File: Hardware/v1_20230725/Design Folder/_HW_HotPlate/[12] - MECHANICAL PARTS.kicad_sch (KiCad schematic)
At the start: 15 parts, among them P1201 CONN_HDR_8POS_2ROW_2.54MM_RA

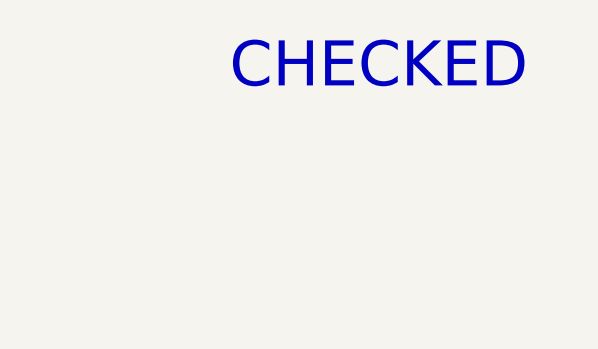
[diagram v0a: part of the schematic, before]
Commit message: Schematic library has been updated
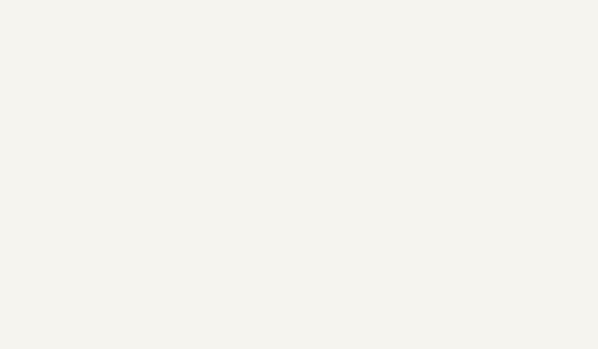
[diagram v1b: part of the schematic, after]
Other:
- note removed: "CHECKED"
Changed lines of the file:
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@@
 (kicad_sch (version 20230121) (generator eeschema)
-  (paper "B")
+  (paper "C")
   (title_block
     (title "Hot Plate")
@@
     (company "Mend0z0")
     (comment 1 "v1")
+    (comment 2 "RELEASED")
     (comment 3 "Siavash Taher Parvar")
     (comment 8 "N/A")
@@
     (effects (font (size 5 5)) (justify left bottom))
   )
-  (text "CHECKED" (at 381 36.83 0)
-    (effects (font (size 5 5)) (justify left bottom))
-  )

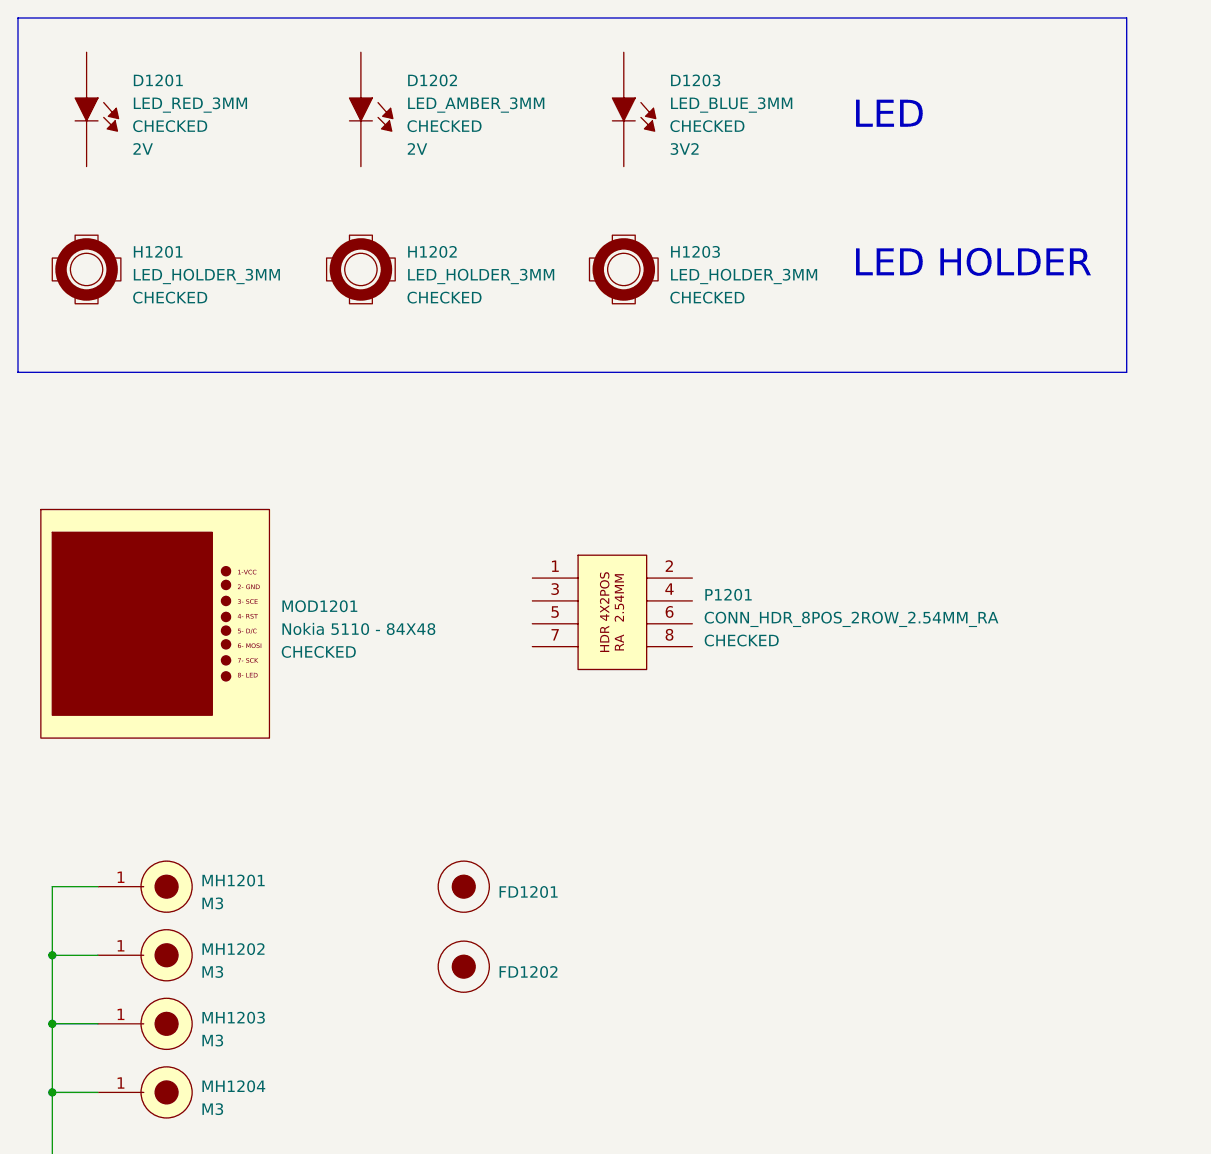
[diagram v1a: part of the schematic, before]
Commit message: components have been updated
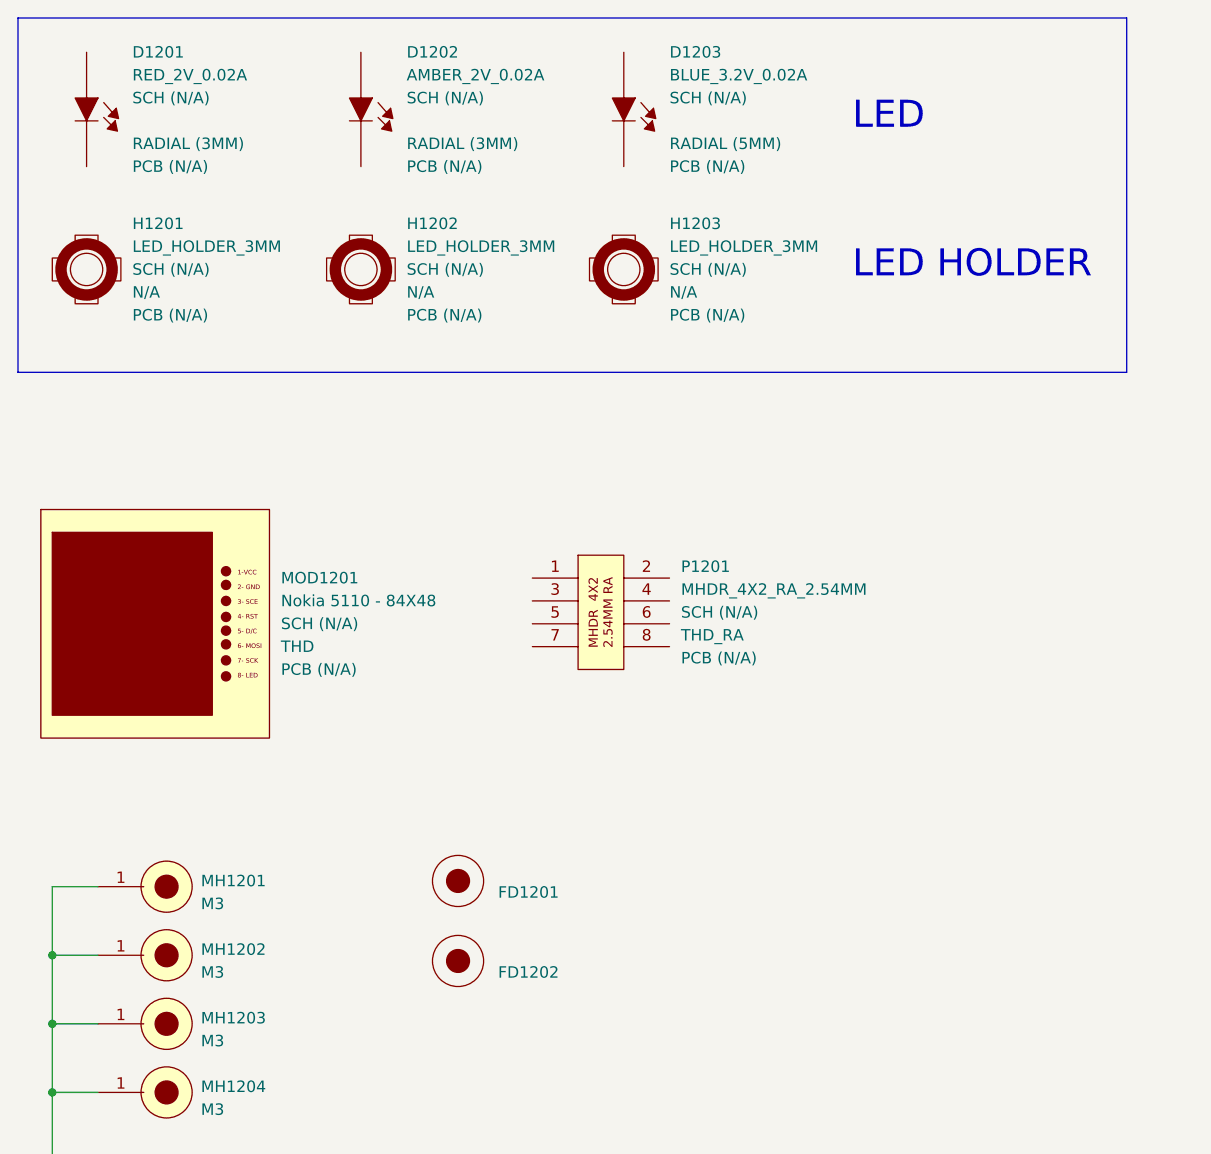
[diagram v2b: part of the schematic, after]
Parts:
- D1201: value LED_RED_3MM -> RED_2V_0.02A; footprint (none) -> LED_THT:LED_D3.0mm; symbol _SCHLIB_HotPlate:MECH_LED_RED_3MM -> _SCHLIB_HotPlate:DIODE_LED_RED_2V_0.02A_627nm_RADIAL (3MM); Manufacturer (none) -> Kingbright; PCB CHECk (none) -> PCB (N/A); Package (none) -> RADIAL (3MM); Part Number WP7113ID -> (none); Part Number (Manufacturer) (none) -> WP7113ID; Part Number (Vendor) (none) -> 754-1264-ND; SCH CHECK CHECKED -> SCH (N/A); Vendor (none) -> Digikey; Voltage 2V -> (none)
- D1202: value LED_AMBER_3MM -> AMBER_2V_0.02A; footprint (none) -> LED_THT:LED_D3.0mm; symbol _SCHLIB_HotPlate:MECH_LED_AMBER_3MM -> _SCHLIB_HotPlate:DIODE_LED_AMBER_2V_0.02A_610nm_RADIAL (3MM); Manufacturer (none) -> American Bright Optoelectronics Corporation; PCB CHECk (none) -> PCB (N/A); Package (none) -> RADIAL (3MM); Part Number BL-BJC1V4V-AT -> (none); Part Number (Manufacturer) (none) -> BL-BJC1V4V-AT; Part Number (Vendor) (none) -> BL-BJC1V4V-AT-ND; SCH CHECK CHECKED -> SCH (N/A); Vendor (none) -> Digikey; Voltage 2V -> (none)
- D1203: value LED_BLUE_3MM -> BLUE_3.2V_0.02A; footprint (none) -> LED_THT:LED_D5.0mm; symbol _SCHLIB_HotPlate:MECH_LED_BLUE_3MM -> _SCHLIB_HotPlate:DIODE_LED_BLUE_3.2V_0.02A_465nm_RADIAL (5MM); Manufacturer (none) -> Würth Elektronik; PCB CHECk (none) -> PCB (N/A); Package (none) -> RADIAL (5MM); Part Number 151051BS04000 -> (none); Part Number (Manufacturer) (none) -> 151051BS04000; Part Number (Vendor) (none) -> 732-5015-ND; SCH CHECK CHECKED -> SCH (N/A); Vendor (none) -> Digikey; Voltage 3V2 -> (none)
- FD1201, FD1202, TXT1201: value ~ -> (none)
- H1201, H1202, H1203: symbol _SCHLIB_HotPlate:MECH_LED_HOLDER -> _SCHLIB_HotPlate:MECH_LED_HOLDER_3MM; Manufacturer (none) -> Lumex Opto/Components Inc.; PCB CHECk (none) -> PCB (N/A); Package (none) -> N/A; Part Number SSH-LX3050 -> (none); Part Number (Manufacturer) (none) -> SSH-LX3050; Part Number (Vendor) (none) -> 67-1330-ND; SCH CHECK CHECKED -> SCH (N/A); Vendor (none) -> Digikey
- MOD1201: Manufacturer (none) -> N/A; PCB CHECk (none) -> PCB (N/A); Package (none) -> THD; Part Number (Vendor) (none) -> 10168; SCH CHECK CHECKED -> SCH (N/A); Vendor (none) -> Sparkfun
- P1201: value CONN_HDR_8POS_2ROW_2.54MM_RA -> MHDR_4X2_RA_2.54MM; footprint (none) -> Connector_PinHeader_2.54mm:PinHeader_2x04_P2.54mm_Horizontal; symbol _SCHLIB_HotPlate:MECH_CONN_HDR_8POS_2ROW_2.54MM_RA -> _SCHLIB_HotPlate:CONN_MHDR_4POS_2ROW_RA_2.54MM; Manufacturer (none) -> SUPERIOR TECH; PCB CHECk (none) -> PCB (N/A); Package (none) -> THD_RA; Part Number PHED-RS008G1ABOGA-C006 -> (none); Part Number (Manufacturer) (none) -> PHED-RS008G1ABOGA-C006; Part Number (Vendor) (none) -> 4324-PHED-RS008G1ABOGA-C006-ND; SCH CHECK CHECKED -> SCH (N/A); Vendor (none) -> Digikey
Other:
- moved on the sheet: FD1201, FD1202, P1201

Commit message: Updating hardware format structure
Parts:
- FD1201, FD1202, TXT1201: value (none) -> ~
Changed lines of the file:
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@@
       (effects (font (size 1.27 1.27)) (justify left))
     )
-    (property "Value" "" (at 76.2 152.4 0)
+    (property "Value" "~" (at 76.2 152.4 0)
       (effects (font (size 1.27 1.27)) (justify left))
     )
@@
       (effects (font (size 1.27 1.27)) (justify left))
     )
-    (property "Value" "" (at 177.8 50.8 0)
+    (property "Value" "~" (at 177.8 50.8 0)
       (effects (font (size 1.27 1.27)) (justify left))
     )
@@
       (effects (font (size 1.27 1.27)) (justify left))
     )
-    (property "Value" "" (at 76.2 143.51 0)
-      (effects (font (size 1.27 1.27)) (justify left))
-    )
+    (property "Value" "~" (at 76.2 143.51 0)
+      (effects (font (size 1.27 1.27)) (justify left))
+    )
